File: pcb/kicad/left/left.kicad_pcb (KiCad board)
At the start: 2 copper layers, 135.9 x 89.5 mm, 61 parts, among them J1 USB_C_Receptacle_USB2.0, J2 AudioJack4, J3 Conn_01x12_Male, SW1 BOOT, SW10 SW_Push, SW12 SW_Push, SW13 SW_Push, SW14 SW_Push, SW15 SW_Push, SW17 SW_Push, SW18 SW_Push, SW19 SW_Push, SW2 RESET, SW21 SW_Push, SW22 SW_Push, SW23 SW_Push, SW24 SW_Push, SW3 SW_Push, SW31 SW_Push, SW32 SW_Push, SW33 SW_Push, SW34 SW_Push, SW4 SW_Push, SW5 SW_Push, SW7 SW_Push, SW8 SW_Push, SW9 SW_Push, U1 STM32, U2 LDO

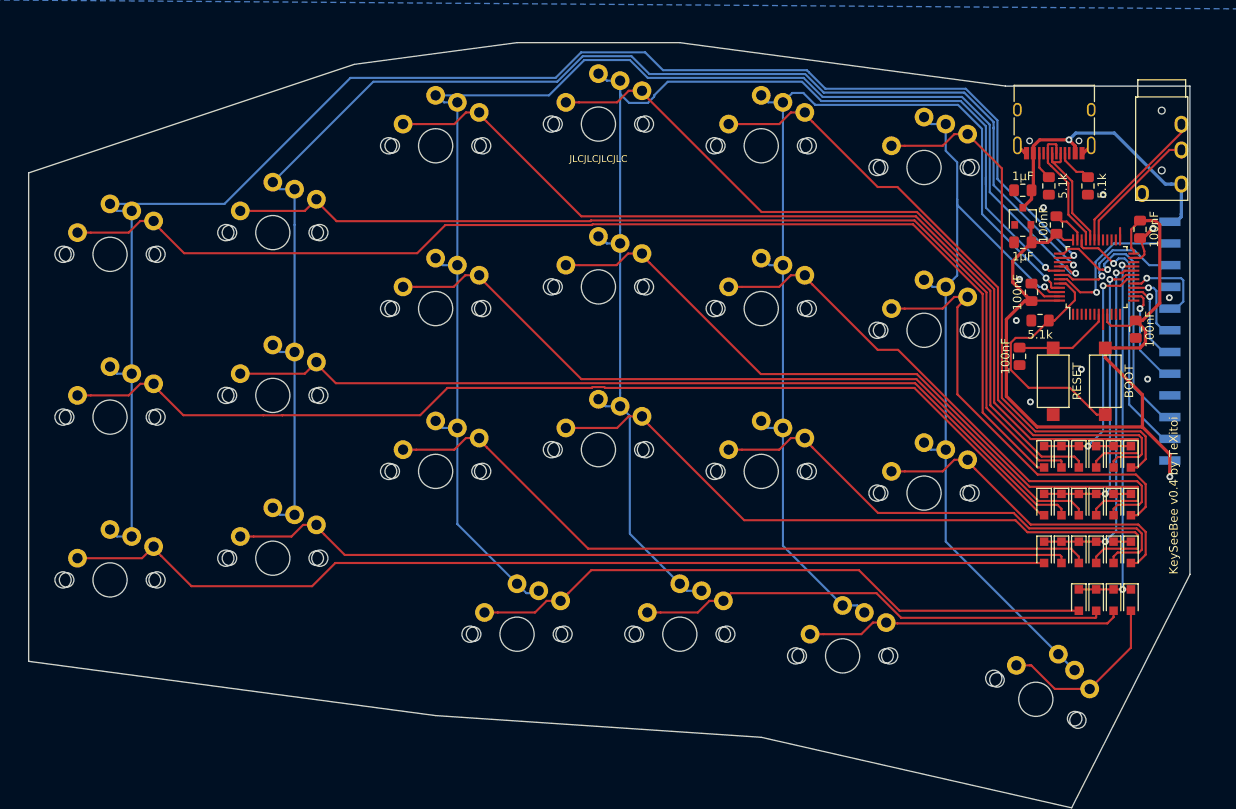
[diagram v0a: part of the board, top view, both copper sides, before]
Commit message: Updated to v0.4.1 with direct wired switches and Rotary Encoders and OLEDS added along with pcb plates
Be warned that the keyplate is missing a cutout for the rotary encoder
and OLED module
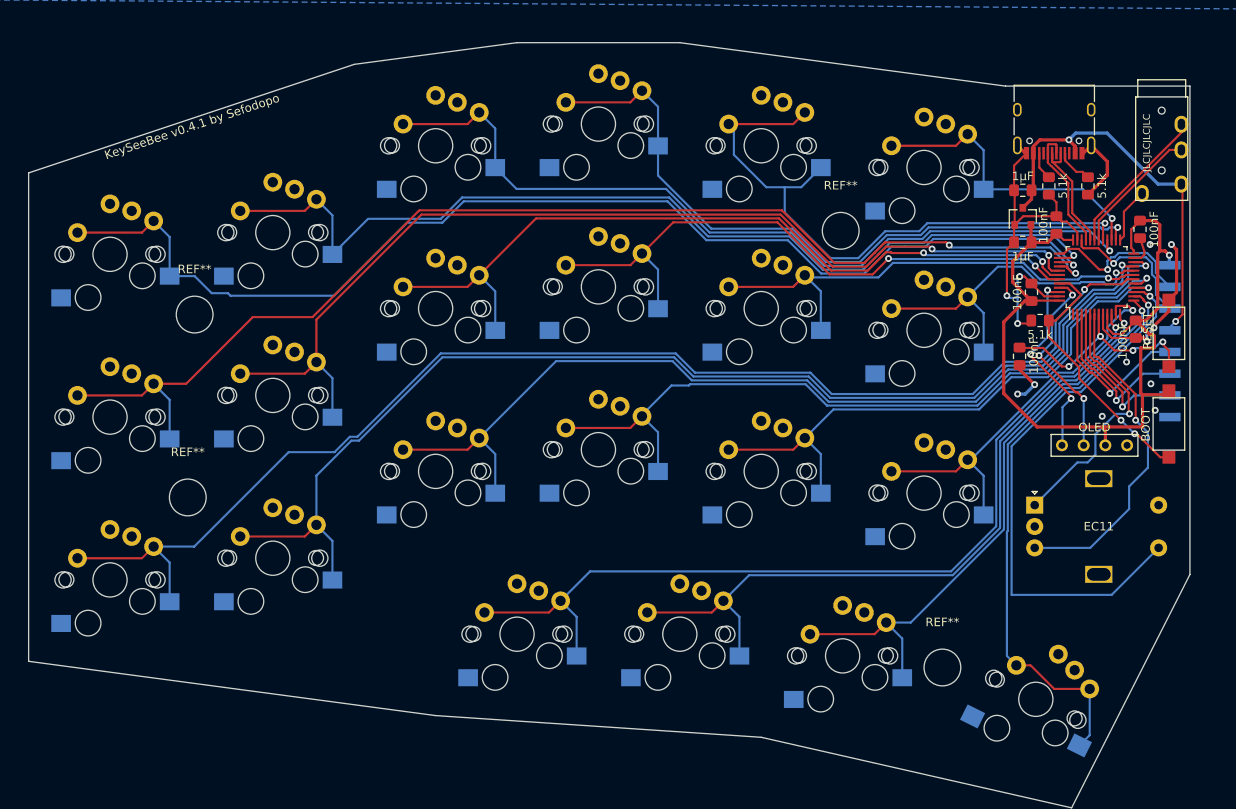
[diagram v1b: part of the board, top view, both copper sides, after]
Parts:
- removed D10, D11, D12, D14, D15, D16, D17, D19, D20, D21, D23, D24, D25, D26, D33, D34, D35, D36, D5, D6, D7, D9: 1N4148WS, Diode_SMD:D_SOD-323_HandSoldering
- added OL1: OLED, foostan-kbd:OLED_1side, F.Cu at (225.7, 89.0)
- added REF**: MountingHole_4.3mm_M4, MountingHole:MountingHole_4.3mm_M4, F.Cu at (199.8, 63.9)
- added REF**: MountingHole_4.3mm_M4, MountingHole:MountingHole_4.3mm_M4, F.Cu at (211.7, 115.0)
- added REF**: MountingHole_4.3mm_M4, MountingHole:MountingHole_4.3mm_M4, F.Cu at (123.4, 95.1)
- added REF**: MountingHole_4.3mm_M4, MountingHole:MountingHole_4.3mm_M4, F.Cu at (124.2, 73.7)
- added SW6: RotaryEncoder_Switch, keebio:RotaryEncoder_Alps_EC11E-Switch_Vertical_H20mm, F.Cu at (230.0, 98.5)
- J3: value Conn_01x12_Male -> Conn_01x08_Male; footprint kicad-harwin:Harwin_M20-89012xx_1x12_P2.54mm_Horizontal -> kicad-harwin:Harwin_M20-89008xx_1x08_P2.54mm_Horizontal
- SW10, SW12, SW13, SW14, SW15, SW17, SW18, SW19, SW21, SW22, SW23, SW24, SW3, SW31, SW32, SW33, SW34, SW4, SW5, SW7, SW8, SW9: footprint custom:CherryMX_Choc_1u -> custom:CherryMX_Choc_MXHotswap_1u
- moved SW2 14.7 mm to (238.2, 75.9), turned to -90 degrees
- moved SW1 8.96 mm to (238.2, 86.5)
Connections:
- net VBAT renamed /VBAT
- J1 pad A8: Net-(J1-PadA8) -> unconnected-(J1-SBU1-PadA8)
- J1 pad B8: Net-(J1-PadB8) -> unconnected-(J1-SBU2-PadB8)
- J3 pad 1: 3.3V -> GND
- J3 pad 2: SWDIO -> PC15
- J3 pad 3: SWDCLK -> PC14
- J3 pad 4: GND -> PC13
- J3 pad 5: PA4 -> 5V
- J3 pad 6: PA5 -> SWDIO
- J3 pad 7: PA6 -> SWDCLK
- J3 pad 8: PA7 -> 3.3V
- SW10 pad 1: Net-(D12-Pad2) -> KEY16
- SW10 pad 2: COL3 -> GND
- SW12 pad 1: Net-(D14-Pad2) -> KEY1
- SW12 pad 2: COL6 -> GND
- SW13 pad 1: Net-(D15-Pad2) -> KEY2
- SW13 pad 2: COL6 -> GND
- SW14 pad 1: Net-(D16-Pad2) -> KEY3
- SW14 pad 2: COL6 -> GND
- SW15 pad 1: Net-(D17-Pad2) -> KEY4
- SW15 pad 2: COL6 -> GND
- SW17 pad 1: Net-(D19-Pad2) -> KEY17
- SW17 pad 2: COL2 -> GND
- SW18 pad 1: Net-(D20-Pad2) -> KEY18
- SW18 pad 2: COL2 -> GND
- SW19 pad 1: Net-(D21-Pad2) -> KEY19
- SW19 pad 2: COL2 -> GND
- SW21 pad 1: Net-(D23-Pad2) -> KEY9
- SW21 pad 2: COL4 -> GND
- SW22 pad 1: Net-(D24-Pad2) -> KEY10
- SW22 pad 2: COL4 -> GND
- SW23 pad 1: Net-(D25-Pad2) -> KEY11
- SW23 pad 2: COL4 -> GND
- SW24 pad 1: Net-(D26-Pad2) -> KEY12
- SW24 pad 2: COL4 -> GND
- SW3 pad 1: Net-(D5-Pad2) -> KEY20
- SW3 pad 2: COL1 -> GND
- SW31 pad 1: Net-(D33-Pad2) -> KEY5
- SW31 pad 2: COL5 -> GND
- SW32 pad 1: Net-(D34-Pad2) -> KEY6
- SW32 pad 2: COL5 -> GND
- SW33 pad 1: Net-(D35-Pad2) -> KEY7
- SW33 pad 2: COL5 -> GND
- SW34 pad 1: Net-(D36-Pad2) -> KEY8
- SW34 pad 2: COL5 -> GND
- SW4 pad 1: Net-(D6-Pad2) -> KEY21
- SW4 pad 2: COL1 -> GND
- SW5 pad 1: Net-(D7-Pad2) -> KEY22
- SW5 pad 2: COL1 -> GND
- SW7 pad 1: Net-(D9-Pad2) -> KEY13
- SW7 pad 2: COL3 -> GND
- SW8 pad 1: Net-(D10-Pad2) -> KEY14
- SW8 pad 2: COL3 -> GND
- SW9 pad 1: Net-(D11-Pad2) -> KEY15
- SW9 pad 2: COL3 -> GND
- U1 pad 10: Net-(U1-Pad10) -> KEY16
- U1 pad 11: Net-(U1-Pad11) -> KEY3
- U1 pad 12: Net-(U1-Pad12) -> KEY12
- U1 pad 13: Net-(U1-Pad13) -> KEY8
- U1 pad 14: PA4 -> KEY4
- U1 pad 15: PA5 -> KEYEXT1
- U1 pad 16: PA6 -> KEY7
- U1 pad 17: PA7 -> KEY11
- U1 pad 18: ROW1 -> KEY22
- U1 pad 19: ROW2 -> KEY6
- U1 pad 2: Net-(U1-Pad2) -> PC13
- U1 pad 20: ROW3 -> KEY2
- U1 pad 21: ROW4 -> KEY19
- U1 pad 22: Net-(U1-Pad22) -> KEY15
- U1 pad 26: Net-(U1-Pad26) -> KEY9
- U1 pad 27: Net-(U1-Pad27) -> KEY1
- U1 pad 28: Net-(U1-Pad28) -> KEY13
- U1 pad 29: Net-(U1-Pad29) -> KEY5
- U1 pad 3: Net-(U1-Pad3) -> PC14
- U1 pad 38: COL1 -> KEY17
- U1 pad 39: COL2 -> KEY20
- U1 pad 4: Net-(U1-Pad4) -> PC15
- U1 pad 40: COL3 -> KEY21
- U1 pad 41: COL4 -> KEY18
- U1 pad 42: PB6 -> KEY14
- U1 pad 43: PB7 -> KEY10
- U1 pad 45: COL5 -> SCL
- U1 pad 46: COL6 -> SDA
- U1 pad 5: Net-(U1-Pad5) -> RE1A
- U1 pad 6: Net-(U1-Pad6) -> REB
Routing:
- net COL1: track 182.5 -> 0.00 mm, vias 1 -> 0
- net COL3: track 164.9 -> 0.00 mm, vias 1 -> 0
- net COL2: track 162.9 -> 0.00 mm, vias 1 -> 0
- net KEY22: track 0.00 -> 150.3 mm, vias 0 -> 1
- net COL4: track 143.4 -> 0.00 mm, vias 1 -> 0
- net KEY21: track 0.00 -> 140.6 mm, vias 0 -> 2
- net Net-(D5-Pad2): track 136.6 -> 0.00 mm
- net KEY20: track 0.00 -> 136.2 mm, vias 0 -> 1
- net KEY19: track 0.00 -> 135.2 mm, vias 0 -> 1
- net Net-(D6-Pad2): track 122.8 -> 0.00 mm
- net COL5: track 122.1 -> 0.00 mm, vias 1 -> 0
- net KEY18: track 0.00 -> 119.2 mm, vias 0 -> 2
- net Net-(D19-Pad2): track 118.1 -> 0.00 mm
- net Net-(D7-Pad2): track 116.8 -> 0.00 mm
- net KEY17: track 0.00 -> 114.2 mm, vias 0 -> 1
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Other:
- net class Default removed
- rule pad_to_mask_clearance: 0 -> 0.038
- board text added: "KeySeeBee v0.4.1 by Sefodopo"
- board text added: "PC13"
- board text added: "PC14"
- board text added: "PC15"
- board text removed: "KeySeeBee v0.4 by TeXitoi"
- board text removed: "PA4"
- board text removed: "PA5"
- board text removed: "PA6"
- board text removed: "PA7"
- board text removed: "PB6"
- board text removed: "PB7"
